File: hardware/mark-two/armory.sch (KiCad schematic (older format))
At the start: 0 parts

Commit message: add USB armory Mk II rev. γ
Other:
- note added: "GPIOs and I2C"
- note added: "REVISIONS (see https://github.com/f-secure-foundry/usbarmory/wiki/Errata-(Mk-II))\n\n- beta (2019-06-25):\n\n - First public release.\n\n- gamma (2021-02-18):\n\n - connect XL1 and XL2 of U11 to GND.\n - Invert UART1 RTS/CTS lines connected to BLE module.\n - Invert UART2 RTS/CTS lines connected to USB-C receptacle.\n - Move BLE module power supply from VLDO3 to SW3.\n - Use VLDO1 (1.8V) to power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"
- note added: "eMMC"
- note removed: "LEDs and I2C"
- note removed: "eMMC 4GB/8GB/16GB"
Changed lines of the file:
@@
 EESchema Schematic File Version 4
-LIBS:armory-cache
 EELAYER 30 0
 EELAYER END
@@
 encoding utf-8
 Sheet 1 13
-Title "USB ARMORY"
-Date "2019-06-25"
-Rev "MARK II"
+Title "USB armory Mk II"
+Date "2021-02-18"
+Rev "γ"
 Comp "F-Secure"
-Comment1 "Copyright © 2019 F-Secure"
-Comment2 "License: CERN OHL v1.2"
-Comment3 "https://github.com/inversepath/usbarmory"
+Comment1 "Copyright © F-Secure Corporation"
+Comment2 "License: CERN-OHL-S"
+Comment3 "https://github.com/f-secure-foundry/usbarmory"
 Comment4 ""
 $EndDescr
@@
 DDR3L RAM 512MB/1GB
 Text Notes 1600 7550 0    150  ~ 0
-eMMC 4GB/8GB/16GB
+eMMC
 Text Notes 1600 9800 0    150  ~ 0
 Secure elements
@@
 Boot configuration
 Text Notes 1600 9050 0    150  ~ 0
-LEDs and I2C
+GPIOs and I2C
 Text Notes 1650 4550 0    150  ~ 0
 i.MX6UL power
@@
 Crystals and UARTs
 Text Notes 11150 3200 0    60   ~ 0
-ESD AND OVERVOLTAGE PROTECTIONS\n\nType-C VBUS overvoltage (20V) protections:\n- All ICs behind ON semiconductor FPF2286 OVP, that can withstand DC inputs up to 28V.\n\nType-C short-to-VBUS protections:\n- USB1 CC/VBUS: unprotected, TUSB320 can withstand only DC inputs from 0 to 6V.\n- USB2 CC1/CC2/VBUS: FUSB303 can withstand DC inputs from 0 to 28V.\n- USB1 and USB2 D+/D- unprotected: short-to-VBUS unlikely (1 pin distance from VBUS pin)\n- Type-C DEBUG pins unprotected: unlikely to connect a power USB device to receptacle;\n   The event should demage the FSA1208 only, keeping the SoC safe.\n\nExposed connectors ESD protections:\n- USB1 CC/D+/D- and USB2 CC1/CC2/D+/D-: TPD4E10\n   (IEC 61000-4-2 Level 4: 12kV Contact Discharge + 15kV Air-Gap Discharge)\n- USB1 and USB2 VBUS: TPD1E10\n   (IEC 61000-4-5 Level 4: 30kV Contact Discharge + 30kV Air-Gap Discharge)\n- USB2 DEBUG pins: TPD8E003\n   (IEC 61000-4-2 Level 4: 12kV Contact Discharge + 15kV Air-Gap Discharge)\n- microSD lines: TPD6F003\n   (IEC 61000-4-2 Level 4: 12kV Contact Discharge + 20kV Air-Gap Discharge)\n- microSD CD: TPD1E10\n   (IEC 61000-4-5 Level 4: 30kV Contact Discharge + 30kV Air-Gap Discharge)\n- microSD Vdd: TPD1E10\n   (IEC 61000-4-5 Level 4: 30kV Contact Discharge + 30kV Air-Gap Discharge)
+ESD AND OVERVOLTAGE PROTECTIONS\n\nType-C VBUS overvoltage (20V) protections:\n- All ICs behind ON semiconductor FPF2286 OVP, that can withstand DC inputs up to 28V.\n\nType-C short-to-VBUS protections:\n- USB1 CC/VBUS: unprotected, TUSB320 can withstand only DC inputs from 0 to 6V.\n- USB2 CC1/CC2/VBUS: FUSB303 can withstand DC inputs from 0 to 28V.\n- USB1 and USB2 D+/D- unprotected: short-to-VBUS unlikely (1 pin distance from VBUS pin)\n- Type-C DEBUG pins unprotected: unlikely to connect a power USB device to receptacle;\n   The event should demage the FSA1208 only, keeping the SoC safe.\n\nExposed connectors ESD protections:\n- USB1 CC/D+/D- and USB2 CC1/CC2/D+/D-: TPD4E10\n   (IEC 61000-4-2 Level 4: 12kV Contact Discharge + 15kV Air-Gap Discharge)\n- USB1 and USB2 VBUS: TPD1E10\n   (IEC 61000-4-5 Level 4: 30kV Contact Discharge + 30kV Air-Gap Discharge)\n- USB2 DEBUG pins: TPD8E003\n   (IEC 61000-4-2 Level 4: 12kV Contact Discharge + 15kV Air-Gap Discharge)\n- microSD lines: TPD6E05U06\n   (IEC 61000-4-2 Level 4: 12kV Contact Discharge + 15kV Air-Gap Discharge)\n- microSD CD: TPD1E10\n   (IEC 61000-4-5 Level 4: 30kV Contact Discharge + 30kV Air-Gap Discharge)\n- microSD Vdd: TPD1E10\n   (IEC 61000-4-5 Level 4: 30kV Contact Discharge + 30kV Air-Gap Discharge)
 Wire Notes Line
 	11050 3250 15750 3250
@@
 Wire Notes Line
 	11050 750  11050 3250
+Text Notes 11125 5375 0    60   ~ 0
+REVISIONS (see https://github.com/f-secure-foundry/usbarmory/wiki/Errata-(Mk-II))\n\n- beta (2019-06-25):\n\n  - First public release.\n\n- gamma (2021-02-18):\n\n  - connect XL1 and XL2 of U11 to GND.\n  - Invert UART1 RTS/CTS lines connected to BLE module.\n  - Invert UART2 RTS/CTS lines connected to USB-C receptacle.\n  - Move BLE module power supply from VLDO3 to SW3.\n  - Use VLDO1 (1.8V) to power eMMC bus interface: NVCC_NAND, eMMC VCCQ and eMMC pull-ups.\n  - Use VLDO3 (3.3V/1.8V) to power microSD bus interfece: NVCC_SD and SD pull-ups.\n  - Replace NXP AT71CH secure element with NXP SE050.\n  - Replace Type-C plug J2 part number.\n  - Lower LED luminosity by increasing the LED resistors R19 and R20 values.\n  - Update U13 p/n with ATECC608B-MAHDA. Do not place on retail units. \n  - Replace U12 p/n with PUSB3TB6AZ.
+Wire Notes Line
+	15750 3500 11050 3500
+Wire Notes Line
+	11050 3700 15750 3700
+Wire Notes Line
+	11050 5525 15750 5525
+Wire Notes Line
+	15750 3500 15750 5525
+Wire Notes Line
+	11050 3500 11050 5525
 $EndSCHEMATC

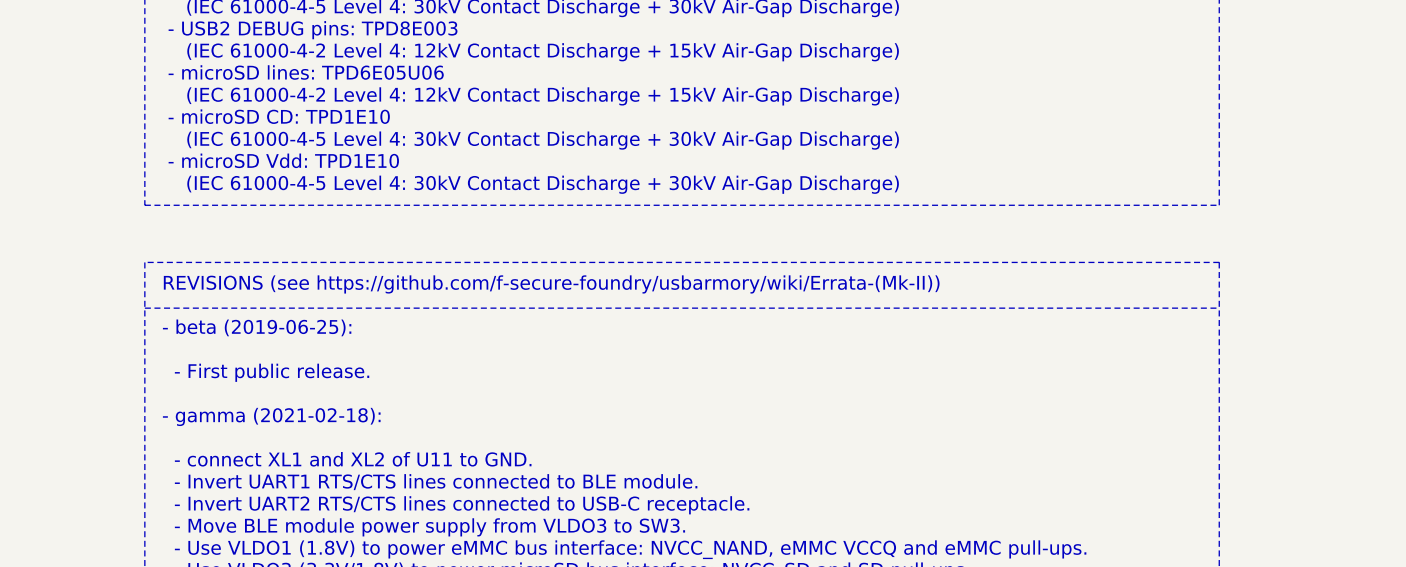
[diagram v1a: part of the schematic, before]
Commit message: rename organization
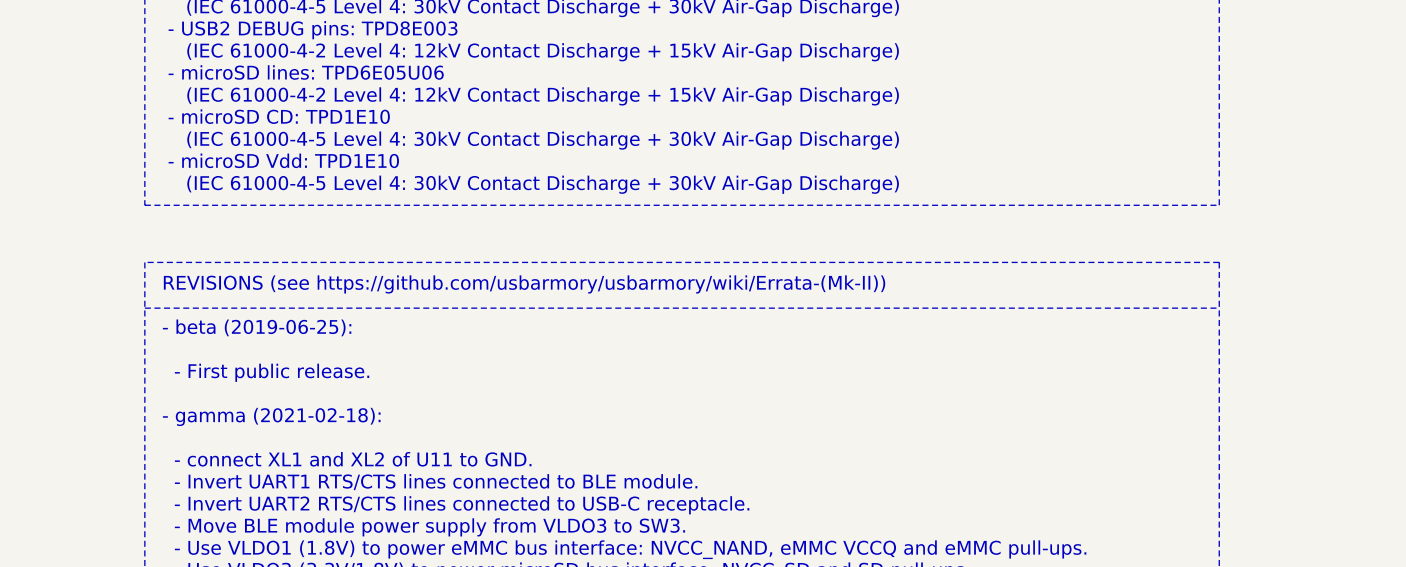
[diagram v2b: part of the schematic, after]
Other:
- note added: "REVISIONS (see https://github.com/usbarmory/usbarmory/wiki/Errata-(Mk-II))\n\n- beta (2019-06-25):\n\n - First public release.\n\n- gamma (2021-02-18):\n\n - connect XL1 and XL2 of U11 to GND.\n - Invert UART1 RTS/CTS lines connected to BLE module.\n - Invert UART2 RTS/CTS lines connected to USB-C receptacle.\n - Move BLE module power supply from VLDO3 to SW3.\n - Use VLDO1 (1.8V) to power eMMC b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"
- note removed: "REVISIONS (see https://github.com/f-secure-foundry/usbarmory/wiki/Errata-(Mk-II))\n\n- beta (2019-06-25):\n\n - First public release.\n\n- gamma (2021-02-18):\n\n - connect XL1 and XL2 of U11 to GND.\n - Invert UART1 RTS/CTS lines connected to BLE module.\n - Invert UART2 RTS/CTS lines connected to USB-C receptacle.\n - Move BLE module power supply from VLDO3 to SW3.\n - Use VLDO1 (1.8V) to power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"
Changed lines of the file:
@@
 Comment1 "Copyright © F-Secure Corporation"
 Comment2 "License: CERN-OHL-S"
-Comment3 "https://github.com/f-secure-foundry/usbarmory"
+Comment3 "https://github.com/usbarmory/usbarmory"
 Comment4 ""
 $EndDescr
@@
 	11050 750  11050 3250
 Text Notes 11125 5375 0    60   ~ 0
-REVISIONS (see https://github.com/f-secure-foundry/usbarmory/wiki/Errata-(Mk-II))\n\n- beta (2019-06-25):\n\n  - First public release.\n\n- gamma (2021-02-18):\n\n  - connect XL1 and XL2 of U11 to GND.\n  - Invert UART1 RTS/CTS lines connected to BLE module.\n  - Invert UART2 RTS/CTS lines connected to USB-C receptacle.\n  - Move BLE module power supply from VLDO3 to SW3.\n  - Use VLDO1 (1.8V) to power eMMC bus interface: NVCC_NAND, eMMC VCCQ and eMMC pull-ups.\n  - Use VLDO3 (3.3V/1.8V) to power microSD bus interfece: NVCC_SD and SD pull-ups.\n  - Replace NXP AT71CH secure element with NXP SE050.\n  - Replace Type-C plug J2 part number.\n  - Lower LED luminosity by increasing the LED resistors R19 and R20 values.\n  - Update U13 p/n with ATECC608B-MAHDA. Do not place on retail units. \n  - Replace U12 p/n with PUSB3TB6AZ.
+REVISIONS (see https://github.com/usbarmory/usbarmory/wiki/Errata-(Mk-II))\n\n- beta (2019-06-25):\n\n  - First public release.\n\n- gamma (2021-02-18):\n\n  - connect XL1 and XL2 of U11 to GND.\n  - Invert UART1 RTS/CTS lines connected to BLE module.\n  - Invert UART2 RTS/CTS lines connected to USB-C receptacle.\n  - Move BLE module power supply from VLDO3 to SW3.\n  - Use VLDO1 (1.8V) to power eMMC bus interface: NVCC_NAND, eMMC VCCQ and eMMC pull-ups.\n  - Use VLDO3 (3.3V/1.8V) to power microSD bus interfece: NVCC_SD and SD pull-ups.\n  - Replace NXP AT71CH secure element with NXP SE050.\n  - Replace Type-C plug J2 part number.\n  - Lower LED luminosity by increasing the LED resistors R19 and R20 values.\n  - Update U13 p/n with ATECC608B-MAHDA. Do not place on retail units. \n  - Replace U12 p/n with PUSB3TB6AZ.
 Wire Notes Line
 	15750 3500 11050 3500
